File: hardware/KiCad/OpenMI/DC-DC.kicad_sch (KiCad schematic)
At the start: 5 parts

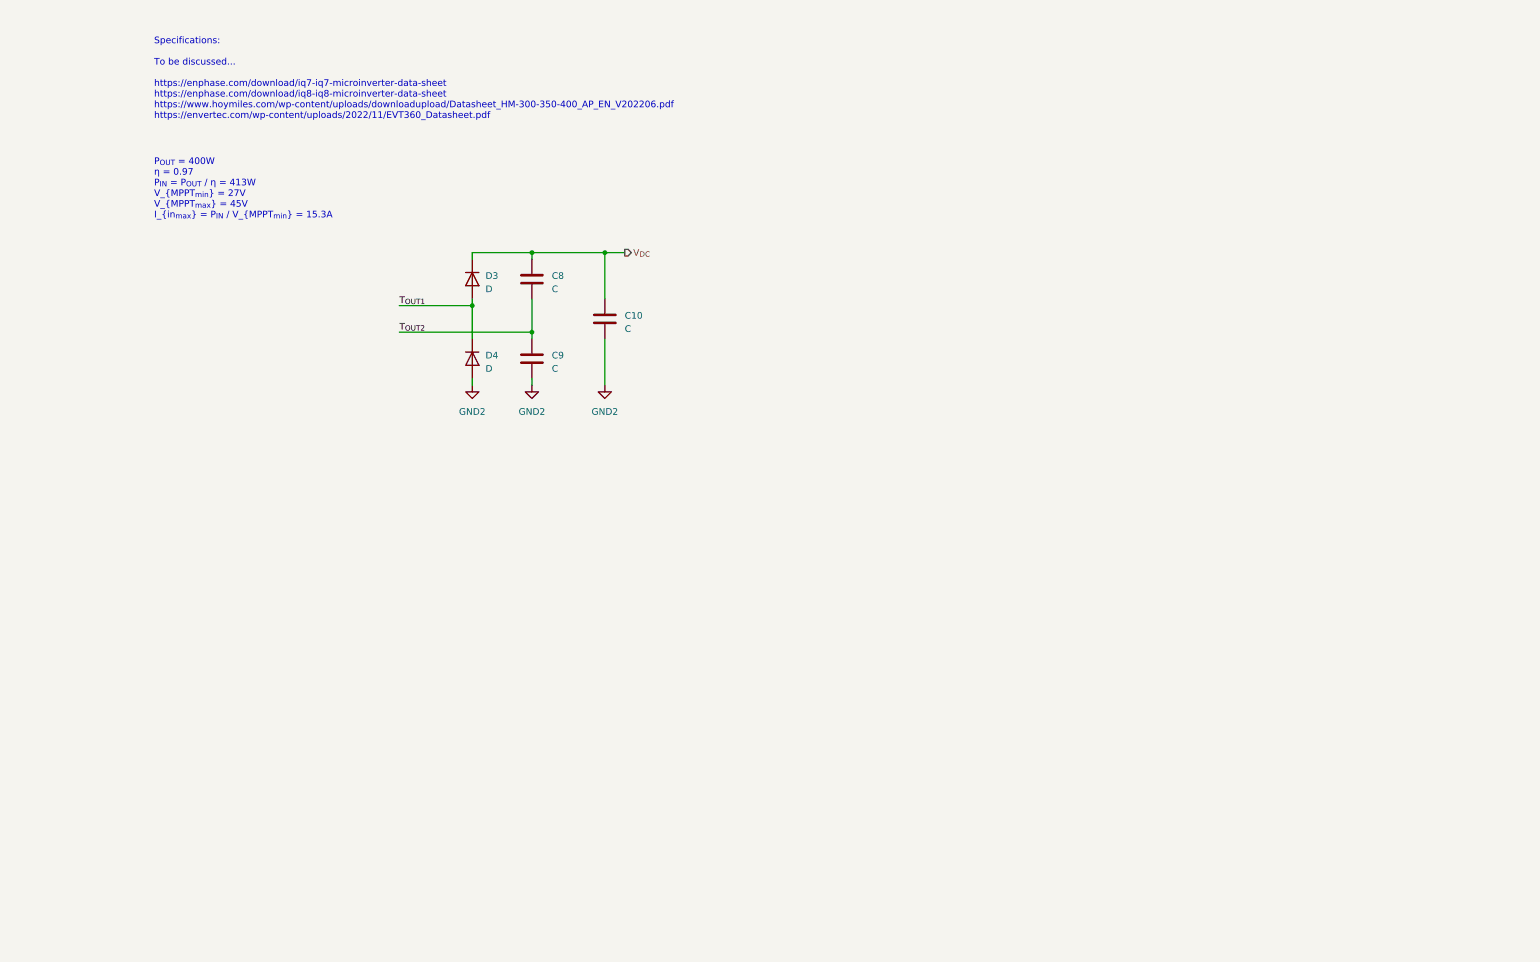
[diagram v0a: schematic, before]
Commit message: feat(hw): Add thoughts for design of input capacitance and inductance
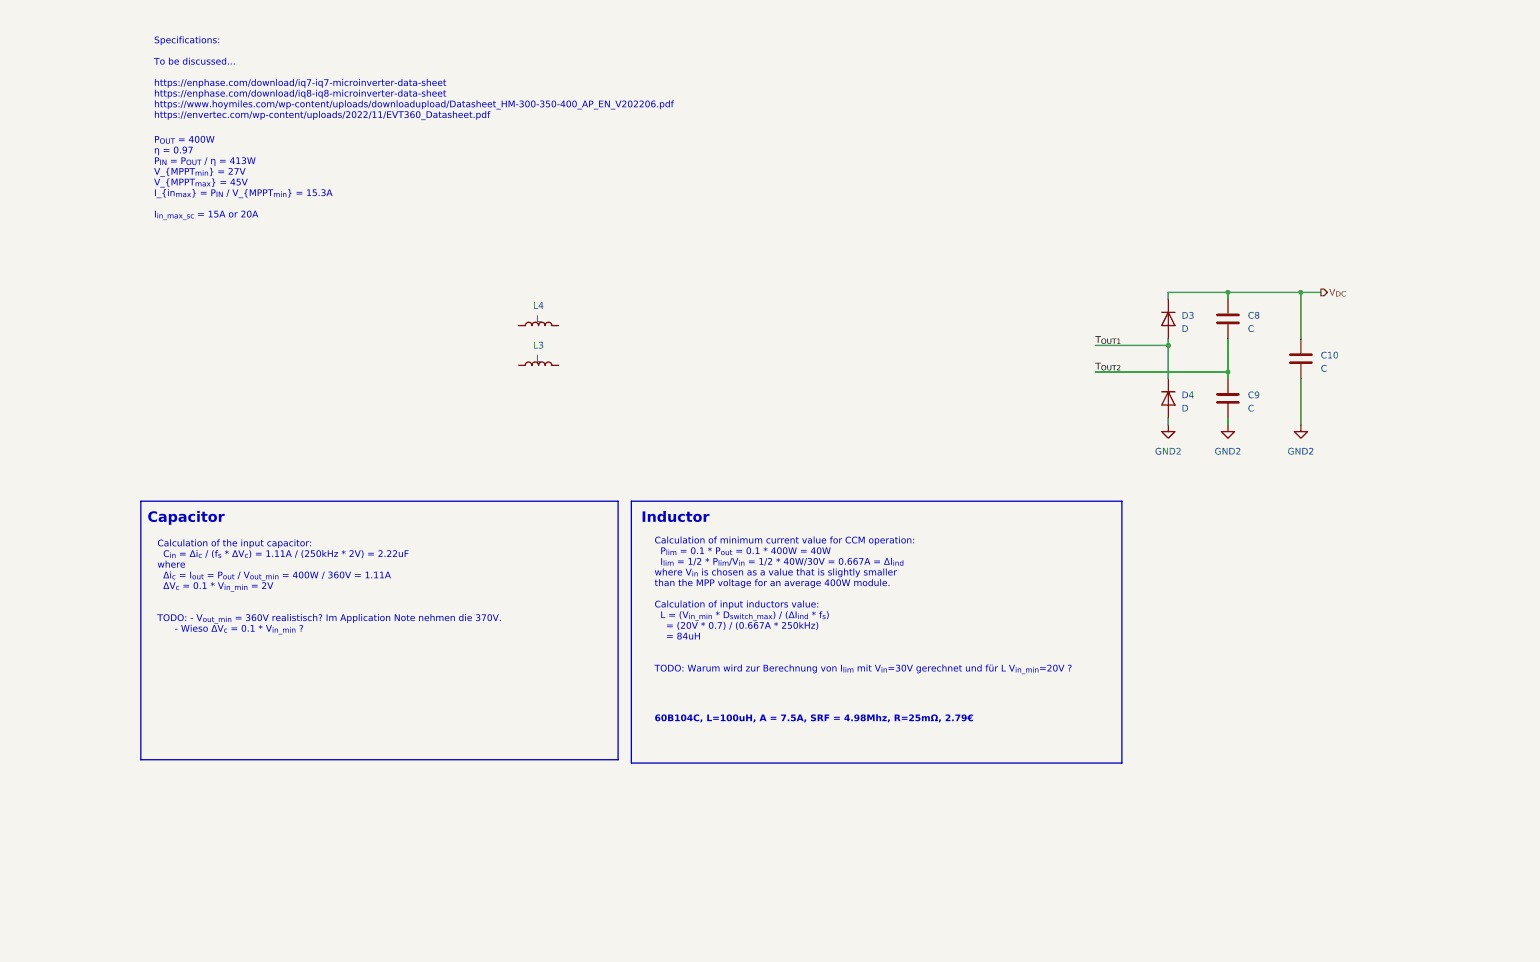
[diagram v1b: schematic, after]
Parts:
- added L3, L4: L, symbol Device:L
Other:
- note added: "60B104C, L=100uH, A = 7.5A, SRF = 4.98Mhz, R=25mΩ, 2.79€"
- note added: "Calculation of minimum current value for CCM operation: P_{lim} = 0.1 * P_{out} = 0.1 * 400W = 40W I_{lim} = 1/2 * P_{lim}/V_{in} = 1/2 * 40W/30V = 0.667A = ΔI_{ind} where V_{in} is chosen as a value that is slightly smaller than the MPP voltage for an average 400W module. Calculation of input inductors value: L = (V_{in_min} * D_{switch_max}) / (ΔI_{ind} * f_{s}) = (20V * 0.7) / (0.667A * 250kHz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"
- note added: "Calculation of the input capacitor: C_{in} = Δi_{c} / (f_{s} * ΔV_{c}) = 1.11A / (250kHz * 2V) = 2.22uF where Δi_{c} = I_{out} = P_{out} / V_{out_min} = 400W / 360V = 1.11A ΔV_{c} = 0.1 * V_{in_min} = 2V TODO: - V_{out_min} = 360V realistisch? Im Application Note nehmen die 370V. - Wieso ΔV_{c} = 0.1 * V_{in_min} ?"
- note added: "Capacitor"
- note added: "Inductor"
- note added: "P_{OUT} = 400W η = 0.97 P_{IN} = P_{OUT} / η = 413W V_{MPPT_{min}} = 27V V_{MPPT_{max}} = 45V I_{in_{max}} = P_{IN} / V_{MPPT_{min}} = 15.3A I_{in_max_sc} = 15A or 20A"
- note removed: "P_{OUT} = 400W η = 0.97 P_{IN} = P_{OUT} / η = 413W V_{MPPT_{min}} = 27V V_{MPPT_{max}} = 45V I_{in_{max}} = P_{IN} / V_{MPPT_{min}} = 15.3A"
- moved on the sheet: C10, C8, C9, D3, D4

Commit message: feat(hw): Add over temperature output
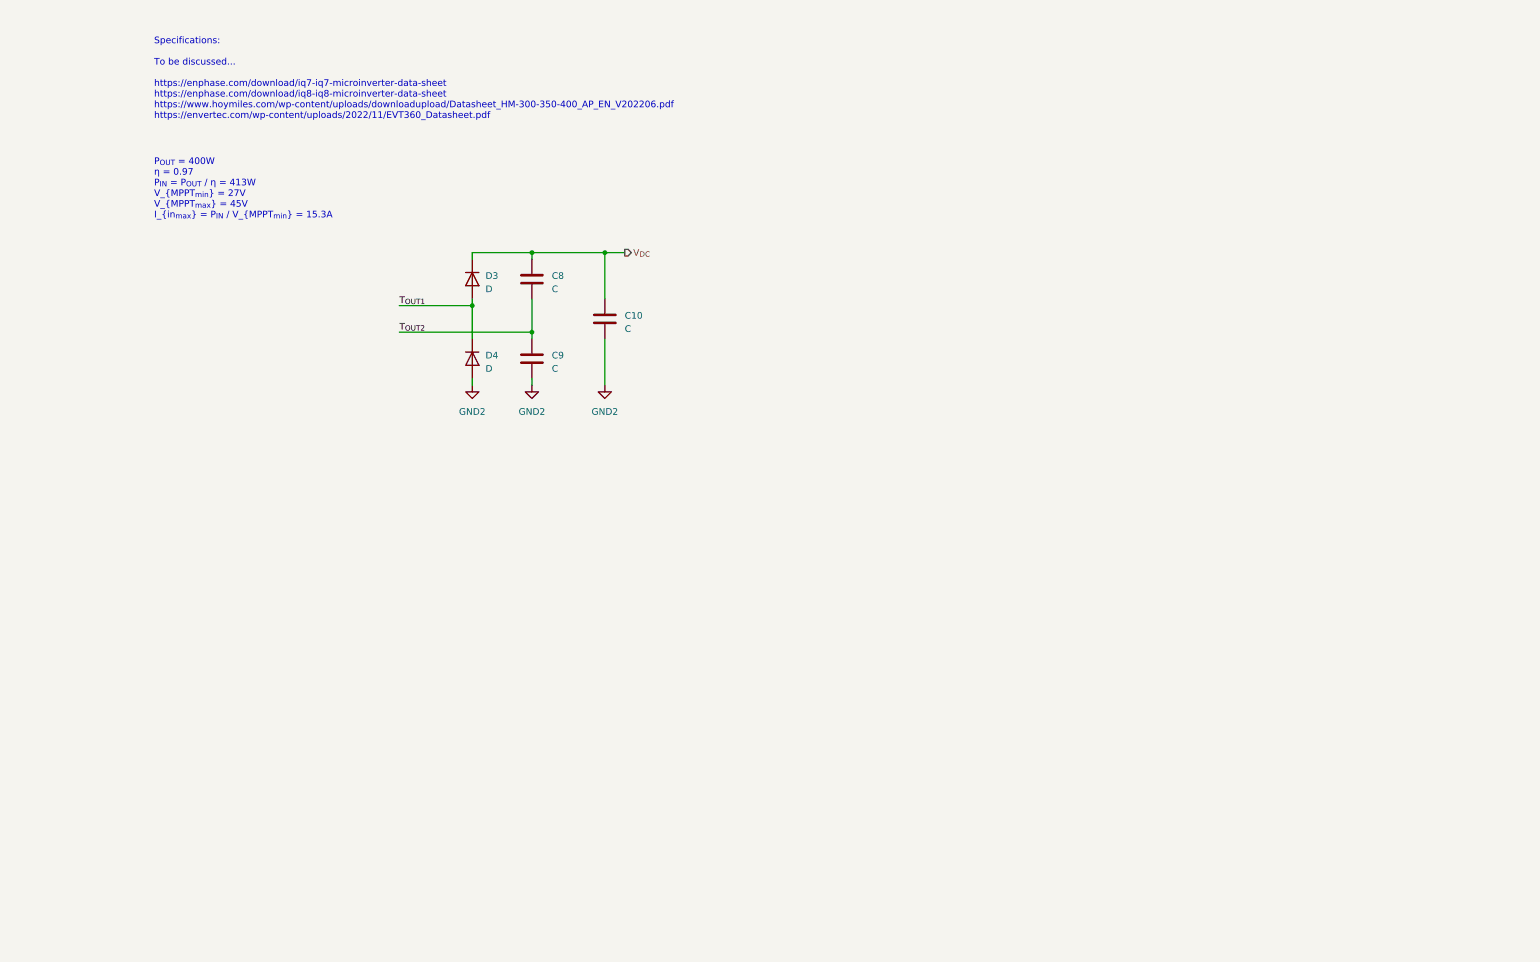
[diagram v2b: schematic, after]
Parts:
- removed L3, L4: L, symbol Device:L
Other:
- note added: "P_{OUT} = 400W η = 0.97 P_{IN} = P_{OUT} / η = 413W V_{MPPT_{min}} = 27V V_{MPPT_{max}} = 45V I_{in_{max}} = P_{IN} / V_{MPPT_{min}} = 15.3A"
- note removed: "60B104C, L=100uH, A = 7.5A, SRF = 4.98Mhz, R=25mΩ, 2.79€"
- note removed: "Calculation of minimum current value for CCM operation: P_{lim} = 0.1 * P_{out} = 0.1 * 400W = 40W I_{lim} = 1/2 * P_{lim}/V_{in} = 1/2 * 40W/30V = 0.667A = ΔI_{ind} where V_{in} is chosen as a value that is slightly smaller than the MPP voltage for an average 400W module. Calculation of input inductors value: L = (V_{in_min} * D_{switch_max}) / (ΔI_{ind} * f_{s}) = (20V * 0.7) / (0.667A * 250kHz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"
- note removed: "Calculation of the input capacitor: C_{in} = Δi_{c} / (f_{s} * ΔV_{c}) = 1.11A / (250kHz * 2V) = 2.22uF where Δi_{c} = I_{out} = P_{out} / V_{out_min} = 400W / 360V = 1.11A ΔV_{c} = 0.1 * V_{in_min} = 2V TODO: - V_{out_min} = 360V realistisch? Im Application Note nehmen die 370V. - Wieso ΔV_{c} = 0.1 * V_{in_min} ?"
- note removed: "Capacitor"
- note removed: "Inductor"
- note removed: "P_{OUT} = 400W η = 0.97 P_{IN} = P_{OUT} / η = 413W V_{MPPT_{min}} = 27V V_{MPPT_{max}} = 45V I_{in_{max}} = P_{IN} / V_{MPPT_{min}} = 15.3A I_{in_max_sc} = 15A or 20A"
- moved on the sheet: C10, C8, C9, D3, D4

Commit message: feat(hw): Add more calculations for inductance
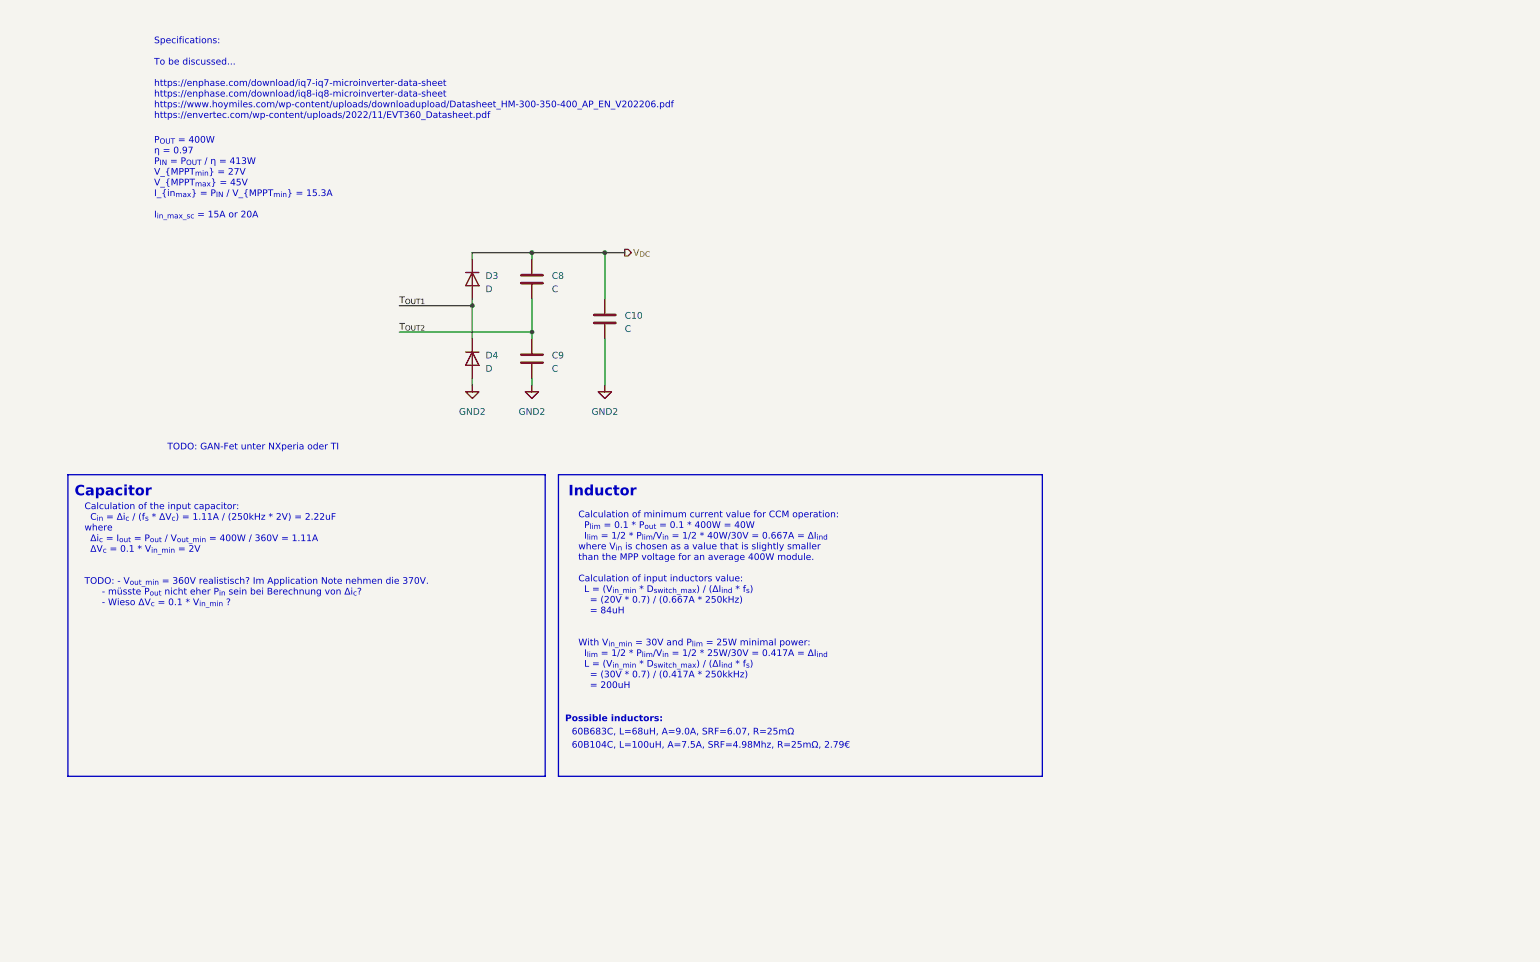
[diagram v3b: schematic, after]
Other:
- note added: "60B104C, L=100uH, A=7.5A, SRF=4.98Mhz, R=25mΩ, 2.79€"
- note added: "60B683C, L=68uH, A=9.0A, SRF=6.07, R=25mΩ"
- note added: "Calculation of minimum current value for CCM operation: P_{lim} = 0.1 * P_{out} = 0.1 * 400W = 40W I_{lim} = 1/2 * P_{lim}/V_{in} = 1/2 * 40W/30V = 0.667A = ΔI_{ind} where V_{in} is chosen as a value that is slightly smaller than the MPP voltage for an average 400W module. Calculation of input inductors value: L = (V_{in_min} * D_{switch_max}) / (ΔI_{ind} * f_{s}) = (20V * 0.7) / (0.667A * 250kHz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"
- note added: "Calculation of the input capacitor: C_{in} = Δi_{c} / (f_{s} * ΔV_{c}) = 1.11A / (250kHz * 2V) = 2.22uF where Δi_{c} = I_{out} = P_{out} / V_{out_min} = 400W / 360V = 1.11A ΔV_{c} = 0.1 * V_{in_min} = 2V TODO: - V_{out_min} = 360V realistisch? Im Application Note nehmen die 370V. - müsste P_{out} nicht eher P_{in} sein bei Berechnung von Δi_{c}? - Wieso ΔV_{c} = 0.1 * V_{in_min} ?"
- note added: "Capacitor"
- note added: "Inductor"
- note added: "P_{OUT} = 400W η = 0.97 P_{IN} = P_{OUT} / η = 413W V_{MPPT_{min}} = 27V V_{MPPT_{max}} = 45V I_{in_{max}} = P_{IN} / V_{MPPT_{min}} = 15.3A I_{in_max_sc} = 15A or 20A"
- note added: "Possible inductors:"
- note added: "TODO: GAN-Fet unter NXperia oder TI"
- note removed: "P_{OUT} = 400W η = 0.97 P_{IN} = P_{OUT} / η = 413W V_{MPPT_{min}} = 27V V_{MPPT_{max}} = 45V I_{in_{max}} = P_{IN} / V_{MPPT_{min}} = 15.3A"
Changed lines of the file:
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@@
     (stroke (width 0) (type default))
   )
-  (text "P_{OUT} = 400W\nη = 0.97\nP_{IN} = P_{OUT} / η = 413W\nV_{MPPT_{min}} = 27V\nV_{MPPT_{max}} = 45V\nI_{in_{max}} = P_{IN} / V_{MPPT_{min}} = 15.3A\n"
+  (rectangle (start 25.4 104.775) (end 116.84 162.56)
+    (stroke (width 0) (type default))
+    (fill (type none))
+  )
+  (rectangle (start 119.38 104.775) (end 212.09 162.56)
+    (stroke (width 0) (type default))
+    (fill (type none))
+  )
+  (text "60B104C, L=100uH, A=7.5A, SRF=4.98Mhz, R=25mΩ, 2.79€"
+    (at 121.92 157.48 0)
+    (effects (font (size 1.27 1.27)) (justify left bottom) (href "https://www.mouser.de/datasheet/2/281/1/kmp_6000b-2936289.pdf"))
+  )
+  (text "TODO: GAN-Fet unter NXperia oder TI" (at 44.45 100.33 0)
+    (effects (font (size 1.27 1.27)) (justify left bottom))
+  )
+  (text "Calculation of minimum current value for CCM operation:\n  P_{lim} = 0.1 * P_{out} = 0.1 * 400W = 40W\n  I_{lim} = 1/2 * P_{lim}/V_{in} = 1/2 * 40W/30V = 0.667A = ΔI_{ind}\nwhere V_{in} is chosen as a value that is slightly smaller\nthan the MPP voltage for an average 400W module.\n\nCalculation of input inductors value:\n  L = (V_{in_min} * D_{switch_max}) / (ΔI_{ind} * f_{s})\n    = (20V * 0.7) / (0.667A * 250kHz)\n    = 84uH\n\n\nWith V_{in_min} = 30V and P_{lim} = 25W minimal power:\n  I_{lim} = 1/2 * P_{lim}/V_{in} = 1/2 * 25W/30V = 0.417A = ΔI_{ind}\n  L = (V_{in_min} * D_{switch_max}) / (ΔI_{ind} * f_{s})\n    = (30V * 0.7) / (0.417A * 250kkHz)\n    = 200uH\n"
+    (at 123.19 146.05 0)
+    (effects (font (size 1.27 1.27)) (justify left bottom))
+  )
+  (text "Possible inductors:" (at 120.65 152.4 0)
+    (effects (font (size 1.27 1.27) (thickness 0.254) bold) (justify left bottom))
+  )
+  (text "Capacitor" (at 26.67 109.22 0)
+    (effects (font (size 2 2) bold) (justify left bottom))
+  )
+  (text "Inductor" (at 121.285 109.22 0)
+    (effects (font (size 2 2) (thickness 0.4) bold) (justify left bottom))
+  )
+  (text "Calculation of the input capacitor:\n  C_{in} = Δi_{c} / (f_{s} * ΔV_{c}) = 1.11A / (250kHz * 2V) = 2.22uF\nwhere \n  Δi_{c} = I_{out} = P_{out} / V_{out_min} = 400W / 360V = 1.11A\n  ΔV_{c} = 0.1 * V_{in_min} = 2V\n\n\nTODO: - V_{out_min} = 360V realistisch? Im Application Note nehmen die 370V.\n      - müsste P_{out} nicht eher P_{in} sein bei Berechnung von Δi_{c}?\n      - Wieso ΔV_{c} = 0.1 * V_{in_min} ?"
+    (at 28.575 130.175 0)
+    (effects (font (size 1.27 1.27)) (justify left bottom))
+  )
+  (text "P_{OUT} = 400W\nη = 0.97\nP_{IN} = P_{OUT} / η = 413W\nV_{MPPT_{min}} = 27V\nV_{MPPT_{max}} = 45V\nI_{in_{max}} = P_{IN} / V_{MPPT_{min}} = 15.3A\n\nI_{in_max_sc} = 15A or 20A\n"
     (at 41.91 55.88 0)
     (effects (font (size 1.27 1.27)) (justify left bottom))
@@
     (effects (font (size 1.27 1.27)) (justify left bottom))
   )
+  (text "60B683C, L=68uH, A=9.0A, SRF=6.07, R=25mΩ" (at 121.92 154.94 0)
+    (effects (font (size 1.27 1.27)) (justify left bottom) (href "https://www.mouser.de/datasheet/2/281/1/kmp_6000b-2936289.pdf"))
+  )
   (label "T_{OUT1}" (at 88.9 72.39 0) (fields_autoplaced)
